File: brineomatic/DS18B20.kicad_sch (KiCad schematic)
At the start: 2 parts, among them J2 Conn_01x03

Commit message: starting to shape up, footprints etc
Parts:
- J3: renamed from J2; footprint (none) -> TerminalBlock_Phoenix:TerminalBlock_Phoenix_PT-1,5-3-3.5-H_1x03_P3.50mm_Horizontal
- renumbered R6 to R8
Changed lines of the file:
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@@
 		(dnp no)
 		(fields_autoplaced yes)
-		(property "Reference" "#PWR07"
+		(property "Reference" "#PWR012"
 			(at 121.92 109.22 0)
 			(effects
@@
 			(project ""
 				(path "/96477ae2-ef08-48f3-8dd4-fe4478541f68/7dc38cc9-02c6-4108-8c2f-d0f758210cae"
-					(reference "#PWR07")
+					(reference "#PWR012")
 					(unit 1)
 				)
@@
 		(dnp no)
 		(fields_autoplaced yes)
-		(property "Reference" "R6"
+		(property "Reference" "R8"
 			(at 127 92.7099 0)
 			(effects
@@
 			(project "brineomatic"
 				(path "/96477ae2-ef08-48f3-8dd4-fe4478541f68/7dc38cc9-02c6-4108-8c2f-d0f758210cae"
-					(reference "R6")
+					(reference "R8")
 					(unit 1)
 				)
@@
 		(dnp no)
 		(fields_autoplaced yes)
-		(property "Reference" "#PWR06"
+		(property "Reference" "#PWR011"
 			(at 121.92 93.98 0)
 			(effects
@@
 			(project ""
 				(path "/96477ae2-ef08-48f3-8dd4-fe4478541f68/7dc38cc9-02c6-4108-8c2f-d0f758210cae"
-					(reference "#PWR06")
+					(reference "#PWR011")
 					(unit 1)
 				)
@@
 		(on_board yes)
 		(dnp no)
-		(property "Reference" "J2"
+		(property "Reference" "J3"
 			(at 113.03 91.186 0)
 			(effects
@@
 			)
 		)
-		(property "Footprint" ""
+		(property "Footprint" "TerminalBlock_Phoenix:TerminalBlock_Phoenix_PT-1,5-3-3.5-H_1x03_P3.50mm_Horizontal"
 			(at 113.03 96.52 0)
 			(effects
@@
 			(project ""
 				(path "/96477ae2-ef08-48f3-8dd4-fe4478541f68/7dc38cc9-02c6-4108-8c2f-d0f758210cae"
-					(reference "J2")
-					(unit 1)
-				)
+					(reference "J3")
+					(unit 1)
+				)

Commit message: starting to look good.
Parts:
- J3: value Conn_01x03 -> DS18B20; footprint TerminalBlock_Phoenix:TerminalBlock_Phoenix_PT-1,5-3-3.5-H_1x03_P3.50mm_Horizontal -> Connector_JST:JST_PH_S3B-PH-K_1x03_P2.00mm_Horizontal
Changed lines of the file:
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@@
 			)
 		)
-		(property "Value" "Conn_01x03"
+		(property "Value" "DS18B20"
 			(at 113.03 90.17 0)
 			(effects
@@
 			)
 		)
-		(property "Footprint" "TerminalBlock_Phoenix:TerminalBlock_Phoenix_PT-1,5-3-3.5-H_1x03_P3.50mm_Horizontal"
+		(property "Footprint" "Connector_JST:JST_PH_S3B-PH-K_1x03_P2.00mm_Horizontal"
 			(at 113.03 96.52 0)
 			(effects

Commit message: updated bom and prepping for Rev A
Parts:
- J3: value DS18B20 -> ~; LCSC (none) -> C157929
- R8: LCSC (none) -> C60816
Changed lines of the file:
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@@
 			)
 		)
-		(property "LCSC" ""
+		(property "LCSC" "C60816"
 			(at 124.46 93.98 0)
 			(effects
@@
 			)
 		)
-		(property "Value" "DS18B20"
+		(property "Value" "~"
 			(at 113.03 90.17 0)
 			(effects
@@
 			(at 113.03 96.52 0)
 			(effects
+				(font
+					(size 1.27 1.27)
+				)
+				(hide yes)
+			)
+		)
+		(property "LCSC" "C157929"
+			(at 113.03 96.52 0)
+			(effects

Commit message: worked on schematic and layout a bit more.
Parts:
- R8: footprint Resistor_SMD:R_0805_2012Metric_Pad1.20x1.40mm_HandSolder -> Resistor_SMD:R_0603_1608Metric
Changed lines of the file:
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@@
 			)
 		)
-		(property "Footprint" "Resistor_SMD:R_0805_2012Metric_Pad1.20x1.40mm_HandSolder"
+		(property "Footprint" "Resistor_SMD:R_0603_1608Metric"
 			(at 124.46 93.98 0)
 			(effects

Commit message: lots of progress on Rev B
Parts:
- J3: value ~ -> THERM
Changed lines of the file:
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@@
 			)
 		)
-		(property "Value" "~"
+		(property "Value" "THERM"
 			(at 113.03 90.17 0)
 			(effects

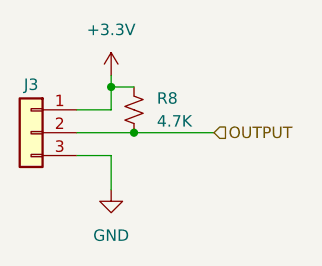
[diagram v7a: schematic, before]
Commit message: tmc2209 driver schematic checked and laid out nicely.
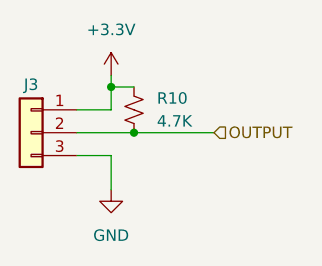
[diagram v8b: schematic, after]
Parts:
- renumbered R8 to R10
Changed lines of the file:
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@@
 		(dnp no)
 		(fields_autoplaced yes)
-		(property "Reference" "#PWR012"
+		(property "Reference" "#PWR014"
 			(at 121.92 109.22 0)
 			(effects
@@
 			(project ""
 				(path "/96477ae2-ef08-48f3-8dd4-fe4478541f68/7dc38cc9-02c6-4108-8c2f-d0f758210cae"
-					(reference "#PWR012")
+					(reference "#PWR014")
 					(unit 1)
 				)
@@
 		(dnp no)
 		(fields_autoplaced yes)
-		(property "Reference" "R8"
+		(property "Reference" "R10"
 			(at 127 92.7099 0)
 			(effects
@@
 			(project "brineomatic"
 				(path "/96477ae2-ef08-48f3-8dd4-fe4478541f68/7dc38cc9-02c6-4108-8c2f-d0f758210cae"
-					(reference "R8")
+					(reference "R10")
 					(unit 1)
 				)
@@
 		(dnp no)
 		(fields_autoplaced yes)
-		(property "Reference" "#PWR011"
+		(property "Reference" "#PWR013"
 			(at 121.92 93.98 0)
 			(effects
@@
 			(project ""
 				(path "/96477ae2-ef08-48f3-8dd4-fe4478541f68/7dc38cc9-02c6-4108-8c2f-d0f758210cae"
-					(reference "#PWR011")
+					(reference "#PWR013")
 					(unit 1)
 				)
